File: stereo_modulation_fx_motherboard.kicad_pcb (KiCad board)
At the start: 2 copper layers, 101.6 x 139.7 mm, 88 parts, among them J1 dry_out_A, J10 Conn_01x04_Male, J11 Conn_01x04_Male, J12 Conn_01x04_Male, J13 Conn_01x03_Male, J2 CV_out_A, J3 wet_in_A, J4 rez_CV_out_A, J5 dry_out_B, J6 CV_out_B, J7 wet_in_B, J8 rez_CV_out_B, SW1 sweep_mode, SW2 invert_B, SW3 DPDT_on_on_on, U1 Teensy3.2, U10 DG419LDY, U11 DG419LDY, U2 CD74HC4067M, U3 MCP4822, U4 MCP4822, U5 TL072, U6 MCP6002-xSN, U7 TL072, U8 MCP6002-xSN, U9 CC3-0512DF-E

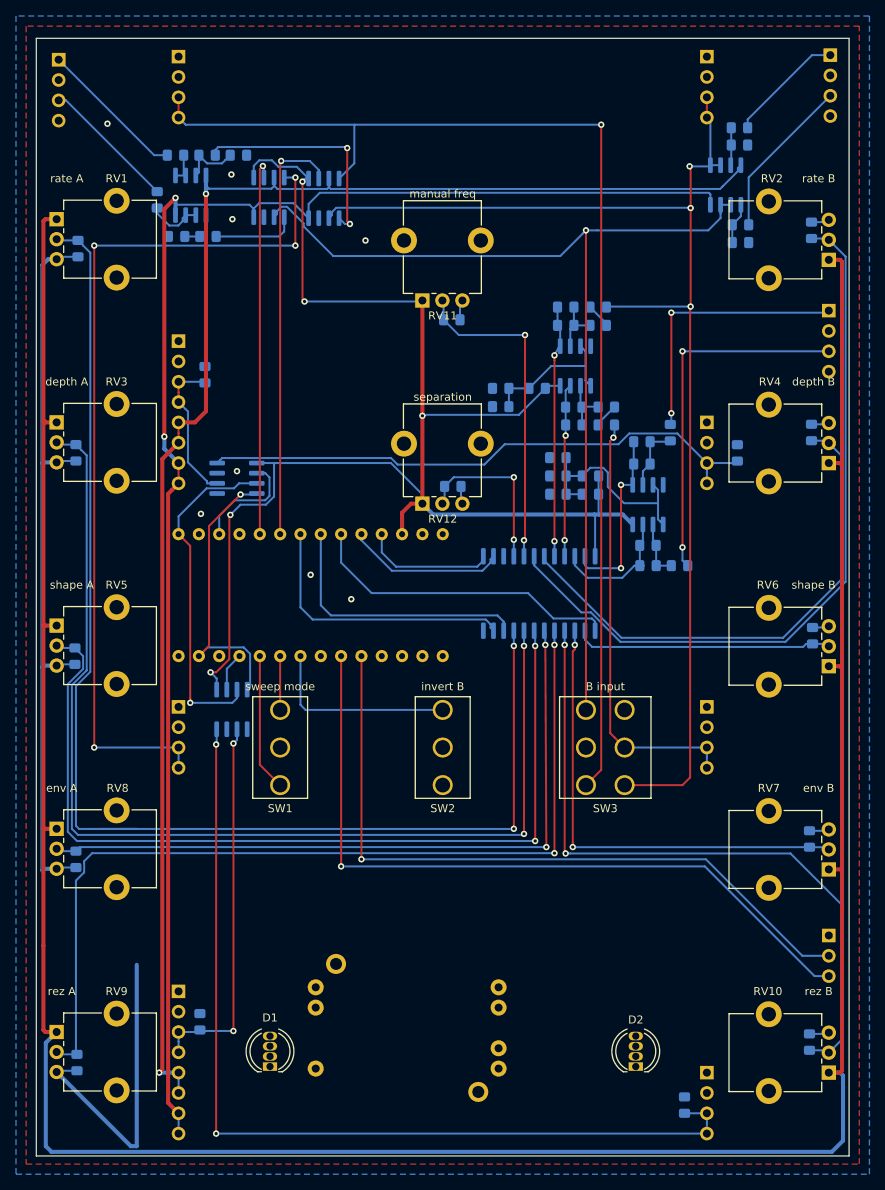
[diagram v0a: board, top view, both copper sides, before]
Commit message: plug in boards are smaller now
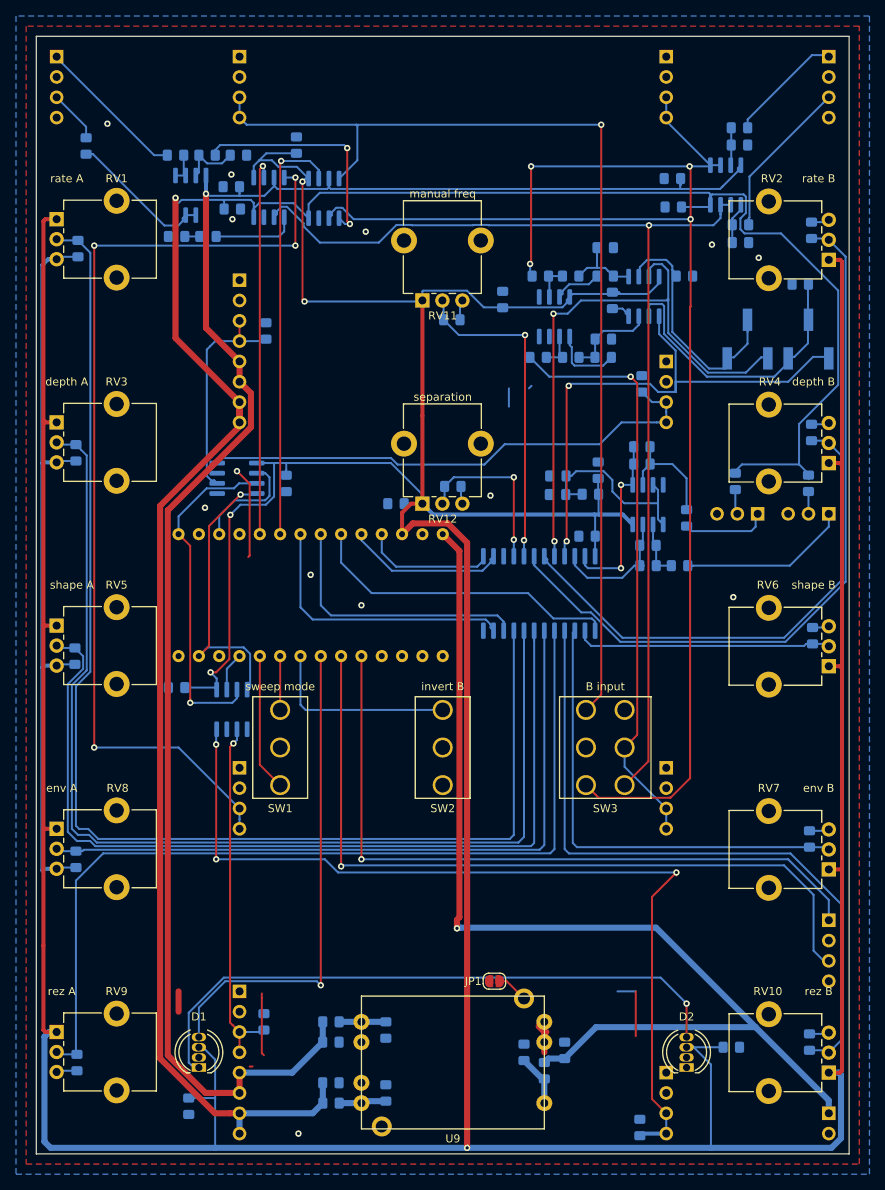
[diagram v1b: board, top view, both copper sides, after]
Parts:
- added C20: C, Capacitor_SMD:C_0805_2012Metric_Pad1.15x1.40mm_HandSolder, B.Cu at (91.4, 152.2)
- added C21: C, Capacitor_SMD:C_0805_2012Metric_Pad1.15x1.40mm_HandSolder, B.Cu at (86.4, 152.4)
- added C22: C, Capacitor_SMD:C_0805_2012Metric_Pad1.15x1.40mm_HandSolder, B.Cu at (69.1, 157.5)
- added C23: C, Capacitor_SMD:C_0805_2012Metric_Pad1.15x1.40mm_HandSolder, B.Cu at (69.1, 149.6)
- added C24: C, Capacitor_SMD:C_0805_2012Metric_Pad1.15x1.40mm_HandSolder, B.Cu at (62.2, 156.2)
- added C25: C, Capacitor_SMD:C_0805_2012Metric_Pad1.15x1.40mm_HandSolder, B.Cu at (62.2, 151.1)
- added C40: C, Capacitor_SMD:C_0805_2012Metric_Pad1.15x1.40mm_HandSolder, B.Cu at (97.4, 58.4)
- added C41: C, Capacitor_SMD:C_0805_2012Metric_Pad1.15x1.40mm_HandSolder, B.Cu at (56.6, 81.3)
- added C42: C, Capacitor_SMD:C_0805_2012Metric_Pad1.15x1.40mm_HandSolder, B.Cu at (42.9, 106.8)
- added C43: C, Capacitor_SMD:C_0805_2012Metric_Pad1.15x1.40mm_HandSolder, B.Cu at (44.5, 159.1)
- added C44: C, Capacitor_SMD:C_0805_2012Metric_Pad1.15x1.40mm_HandSolder, B.Cu at (112.3, 151.8)
- added C45: C, Capacitor_SMD:C_0805_2012Metric_Pad1.15x1.40mm_HandSolder, B.Cu at (57.9, 39.0)
- added C5: 4u7, Capacitor_SMD:C_0805_2012Metric_Pad1.15x1.40mm_HandSolder, B.Cu at (96.3, 63.2)
- added C6: 4u7, Capacitor_SMD:C_0805_2012Metric_Pad1.15x1.40mm_HandSolder, B.Cu at (96.5, 51.8)
- added C7: C, Capacitor_SMD:C_0805_2012Metric_Pad1.15x1.40mm_HandSolder, B.Cu at (94.2, 87.9)
- added C8: C, Capacitor_SMD:C_0805_2012Metric_Pad1.15x1.40mm_HandSolder, B.Cu at (105.0, 46.7)
- added C9: C, Capacitor_SMD:C_0805_2012Metric_Pad1.15x1.40mm_HandSolder, B.Cu at (104.9, 43.2)
- added J14: Conn_01x03_Male, Connector_PinHeader_2.54mm:PinHeader_1x03_P2.54mm_Vertical, B.Cu at (124.5, 85.1)
- added J9: +5_volts_in, Connector_PinHeader_2.54mm:PinHeader_1x02_P2.54mm_Vertical, B.Cu at (124.5, 160.0)
- added JP1: Jumper_NO_Small, Jumper:SolderJumper-2_P1.3mm_Open_RoundedPad1.0x1.5mm, F.Cu at (82.7, 143.5)
- added L1: L, Inductor_SMD:L_0805_2012Metric_Pad1.15x1.40mm_HandSolder, B.Cu at (88.9, 154.7)
- added L2: L, Inductor_SMD:L_0805_2012Metric_Pad1.15x1.40mm_HandSolder, B.Cu at (62.2, 158.8)
- added L3: L, Inductor_SMD:L_0805_2012Metric_Pad1.15x1.40mm_HandSolder, B.Cu at (62.2, 148.6)
- added R21: 2k2, Resistor_SMD:R_0805_2012Metric_Pad1.15x1.40mm_HandSolder, B.Cu at (120.9, 56.4)
- added R22: 2k2, Resistor_SMD:R_0805_2012Metric_Pad1.15x1.40mm_HandSolder, B.Cu at (106.4, 55.4)
- added RV13: 100k, Potentiometer_SMD:Potentiometer_Bourns_3269W_Vertical, B.Cu at (121.9, 63.2)
- added RV14: 100k, Potentiometer_SMD:Potentiometer_Bourns_3269W_Vertical, B.Cu at (114.3, 63.2)
- added U12: MCP6002-xSN, Package_SO:SOIC-8_3.9x4.9mm_P1.27mm, B.Cu at (101.3, 57.9)
- C32: value 100nF -> C
- J12: value Conn_01x04_Male -> Conn_01x03_Male; footprint Connector_PinHeader_2.54mm:PinHeader_1x04_P2.54mm_Vertical -> Connector_PinHeader_2.54mm:PinHeader_1x03_P2.54mm_Vertical
- J13: value Conn_01x03_Male -> Conn_01x04_Male; footprint Connector_PinHeader_2.54mm:PinHeader_1x03_P2.54mm_Vertical -> Connector_PinHeader_2.54mm:PinHeader_1x04_P2.54mm_Vertical
- R10, R9: value ??? -> 10k
- R11, R12: value 10k -> 30k
- R3, R4: value ??? -> 20k
- SW1: value sweep_mode -> sweep_mode_center_off
- SW3: value DPDT_on_on_on -> B_input_selector_on_on_on
- U9: moved to F.Cu
- moved C33 55.5 mm to (49.8, 44.2), turned to 180 degrees
- moved C32 40.3 mm to (49.9, 47.0), turned to 0 degrees
- moved C34 35.3 mm to (70.4, 83.8), turned to 180 degrees
- moved R20 31.3 mm to (121.9, 81.3), turned to 270 degrees
- moved J12 26.9 mm to (115.6, 85.1), turned to 90 degrees
- moved R12 20.9 mm to (96.5, 55.4)
- moved C36 20.8 mm to (95.6, 79.6), turned to 90 degrees
- moved R4 18.3 mm to (88.4, 55.4), turned to 180 degrees
- moved R19 18.1 mm to (112.8, 81.0), turned to 270 degrees
- moved C35 18.0 mm to (83.7, 58.3), turned to 90 degrees
- moved R10 16.4 mm to (92.2, 55.4), turned to 180 degrees
- moved C2 14.7 mm to (101.1, 68.8)
- moved R8 11.2 mm to (31.6, 39.1)
- moved R14 10.9 mm to (106.7, 85.6), turned to 270 degrees
- moved J7 10.8 mm to (50.8, 116.8)
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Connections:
- C1 pad 2: GNDA -> Vin-
- C10 pad 2: GNDA -> Vin-
- C11 pad 2: GNDA -> Vin-
- C12 pad 2: GNDA -> Vin-
- C13 pad 2: GNDA -> Vin-
- C14 pad 2: GNDA -> Vin-
- C15 pad 2: GNDA -> Vin-
- C16 pad 2: GNDA -> Vin-
- C17 pad 2: GNDA -> Vin-
- C18 pad 2: GNDA -> Vin-
- C19 pad 2: GNDA -> Vin-
- C2 pad 2: GNDA -> Vin-
- C28 pad 1: env_A -> env_level_A
- C28 pad 2: GNDA -> Vin-
- C29 pad 1: env_B -> env_level_B
- C29 pad 2: GNDA -> Vin-
- C3 pad 2: GNDA -> Vin-
- C32 pad 1: audio_to_uC_amp_bias -> +12V
- C32 pad 2: GNDA -> Vin-
- C33 pad 1: Net-(C33-Pad1) -> -12V
- C33 pad 2: dry_B -> Vin-
- C34 pad 1: Net-(C34-Pad1) -> +3V3
- C34 pad 2: dry_A -> Vin-
- C35 pad 1: B_to_uC -> +3V3
- C35 pad 2: Net-(C35-Pad2) -> Vin-
- C36 pad 1: A_to_uC -> +3V3
- C36 pad 2: Net-(C36-Pad2) -> Vin-
- C39 pad 2: GNDA -> Vin-
- C4 pad 2: GNDA -> Vin-
- D1 pad 2: GNDA -> Vin-
- D2 pad 2: GNDA -> Vin-
- J1 pad 1: GNDA -> Vin-
- J1 pad 2: GNDA -> Vin-
- J10 pad 2: GNDA -> Vin-
- J10 pad 4: GNDA -> Vin-
- J11 pad 2: GNDA -> Vin-
- J11 pad 4: GNDA -> Vin-
- J12 pad 2: GNDA -> Net-(J12-Pad2)
- J12 pad 3: freq_CV_in -> Vin-
- J13 pad 1: GNDA -> footswitch_A
- J13 pad 2: footswitch_A -> Vin-
- J2 pad 1: GNDA -> Vin-
- J2 pad 2: GNDA -> Vin-
- J3 pad 1: GNDA -> Vin-
- J3 pad 2: GNDA -> Vin-
- J4 pad 1: GNDA -> Vin-
- J4 pad 2: GNDA -> Vin-
- J5 pad 1: GNDA -> Vin-
- J5 pad 2: GNDA -> Vin-
- J6 pad 1: GNDA -> Vin-
- J6 pad 2: GNDA -> Vin-
- J7 pad 1: GNDA -> Vin-
- J7 pad 2: GNDA -> Vin-
- J8 pad 1: GNDA -> Vin-
- J8 pad 2: GNDA -> Vin-
- R1 pad 2: GNDA -> Vin-
- R10 pad 1: B_to_uC -> Net-(C6-Pad1)
- R10 pad 2: Net-(C35-Pad2) -> Net-(R10-Pad2)
- R11 pad 1: +3V3 -> Net-(C5-Pad1)
- R11 pad 2: audio_to_uC_amp_bias -> Net-(R11-Pad2)
- R12 pad 1: audio_to_uC_amp_bias -> Net-(C6-Pad1)
- R12 pad 2: GNDA -> Net-(R12-Pad2)
- R18 pad 2: GNDA -> Vin-
- R19 pad 1: +3V3 -> +12V
- R19 pad 2: CV_amp_bias -> Net-(J12-Pad2)
- R2 pad 2: GNDA -> Vin-
- R20 pad 1: CV_amp_bias -> +12V
- R20 pad 2: GNDA -> Net-(J14-Pad2)
- R3 pad 1: Net-(C36-Pad2) -> Net-(R3-Pad1)
- R3 pad 2: Net-(C34-Pad1) -> dry_B
- R4 pad 1: Net-(C35-Pad2) -> Net-(R10-Pad2)
- R4 pad 2: Net-(C33-Pad1) -> dry_A
- R5 pad 2: GNDA -> Vin-
- R6 pad 2: GNDA -> Vin-
- R9 pad 1: A_to_uC -> Net-(C5-Pad1)
- R9 pad 2: Net-(C36-Pad2) -> Net-(R3-Pad1)
- RV1 pad 3: GNDA -> Vin-
- RV10 pad 3: GNDA -> Vin-
- RV11 pad 3: GNDA -> Vin-
- RV12 pad 3: GNDA -> Vin-
- RV2 pad 3: GNDA -> Vin-
- RV3 pad 3: GNDA -> Vin-
- RV4 pad 3: GNDA -> Vin-
- RV5 pad 3: GNDA -> Vin-
- RV6 pad 3: GNDA -> Vin-
- RV7 pad 2: env_B -> env_level_B
- RV7 pad 3: GNDA -> Vin-
- RV8 pad 2: env_A -> env_level_A
- RV8 pad 3: GNDA -> Vin-
- RV9 pad 3: GNDA -> Vin-
- SW1 pad 2: GNDA -> Vin-
- SW2 pad 2: GNDA -> Vin-
- SW3 pad 1: dry_A -> Net-(SW3-Pad1)
- SW3 pad 4: wet_A -> dry_A
- SW3 pad 6: Net-(SW3-Pad6) -> wet_A
- U1 pad 1: GNDA -> Vin-
- U1 pad 32: GNDA -> Vin-
- U1 pad 33: Net-(U1-Pad33) -> Vin+
- U10 pad 3: GNDA -> Vin-
- U11 pad 2: Net-(SW3-Pad6) -> Net-(SW3-Pad1)
- U11 pad 3: GNDA -> Vin-
- U2 pad 12: GNDA -> Vin-
- U2 pad 15: GNDA -> Vin-
- U2 pad 20: A_to_uC -> env_A
- U2 pad 21: B_to_uC -> env_B
- U2 pad 3: env_B -> env_level_B
- U2 pad 6: env_A -> env_level_A
- U3 pad 5: GNDA -> Vin-
- U3 pad 7: GNDA -> Vin-
- U4 pad 5: GNDA -> Vin-
- U4 pad 7: GNDA -> Vin-
- U6 pad 4: GNDA -> Vin-
- U7 pad 6: Net-(SW3-Pad6) -> Net-(SW3-Pad1)
- U7 pad 7: Net-(SW3-Pad6) -> Net-(SW3-Pad1)
- U8 pad 1: A_to_uC -> Net-(R11-Pad2)
- U8 pad 2: Net-(C36-Pad2) -> Net-(R3-Pad1)
- U8 pad 3: audio_to_uC_amp_bias -> Vin-
- U8 pad 4: GNDA -> Vin-
- U8 pad 5: audio_to_uC_amp_bias -> Vin-
- U8 pad 6: Net-(C35-Pad2) -> Net-(R10-Pad2)
- U8 pad 7: B_to_uC -> Net-(R12-Pad2)
- U9 pad 2: Net-(C20-Pad2) -> Vin-
- U9 pad 3: Net-(C20-Pad2) -> Vin-
- U9 pad 5: GNDA -> Vin-
- U9 pad 8: (no net) -> Net-(JP1-Pad1)
- U9 pad 9: (no net) -> Net-(U9-Pad9)
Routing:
- net Vin-: track 0.00 -> 151.4 mm, vias 0 -> 13
- net +3V3: track 531.1 -> 681.0 mm
- net GNDA: track 148.8 -> 0.00 mm, vias 8 -> 0
- net Vin+: track 0.00 -> 135.5 mm, vias 0 -> 1
- net Net-(SW3-Pad1): track 0.00 -> 134.3 mm, vias 0 -> 1
- net Net-(SW3-Pad6): track 124.2 -> 0.00 mm, vias 1 -> 0
- net +12V: track 196.7 -> 289.4 mm, vias 2 -> 1
- net env_level_A: track 0.00 -> 88.4 mm
- net Net-(D1-Pad1): track 0.00 -> 77.2 mm, vias 0 -> 1
- net LED_serial: track 0.00 -> 61.5 mm, vias 0 -> 1
- net env_level_B: track 0.00 -> 58.9 mm
- net Net-(R21-Pad1): track 0.00 -> 36.7 mm
- net A_to_uC: track 31.5 -> 0.00 mm, vias 2 -> 0
- net dry_A: track 154.6 -> 186.1 mm, vias 3 -> 4
- net Net-(R22-Pad1): track 0.00 -> 31.3 mm
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- added copper zone on B.Cu, net Vin-
- added copper zone on F.Cu, net Vin-
- removed copper zone on B.Cu, net GNDA
- removed copper zone on F.Cu, net GNDA
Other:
- board text added: "+"
- board text added: "-"
- board text added: "5V in"
- board text added: "R"
- board text added: "S"
- board text added: "T"
- board text added: "V+"
- board text added: "V-"
- board text added: "dry A"
- board text added: "dry B"
- board text added: "env A trim"
- board text added: "env B trim"
- board text added: "freq CV A"
- board text added: "freq CV B"
- board text added: "rez CV A"
- board text added: "rez CV B"
- board text added: "wet A"
- board text added: "wet B"

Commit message: tidy schematic, add stitching vias
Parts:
- added C46: C, Capacitor_SMD:C_0805_2012Metric_Pad1.15x1.40mm_HandSolder, B.Cu at (54.4, 159.0)
- added C47: C, Capacitor_SMD:C_0805_2012Metric_Pad1.15x1.40mm_HandSolder, B.Cu at (57.1, 156.0)
- C32, C33, C34, C35, C36, C40, C41, C42, C43, C44, C45, C7, C8, C9: value C -> 100nF
- moved J12 1.27 mm to (114.3, 85.1)
- moved R14 0.76 mm to (105.9, 85.6)
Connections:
- net CV_out_A renamed freq_CV_A
- net CV_out_B renamed freq_CV_B
- net rez_CV_out_A renamed rez_CV_A
- net rez_CV_out_B renamed rez_CV_B
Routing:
- net Net-(C37-Pad2): track 15.0 -> 13.5 mm
- net LFO_rate_CV_in: track 10.2 -> 9.66 mm
- net Vin-: vias 13 -> 169
